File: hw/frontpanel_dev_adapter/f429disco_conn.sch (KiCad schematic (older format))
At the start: 7 parts, among them J601 Conn_02x32_Odd_Even, J602 Conn_02x32_Odd_Even, J603 Conn_02x32_Odd_Even, J604 Conn_02x32_Odd_Even

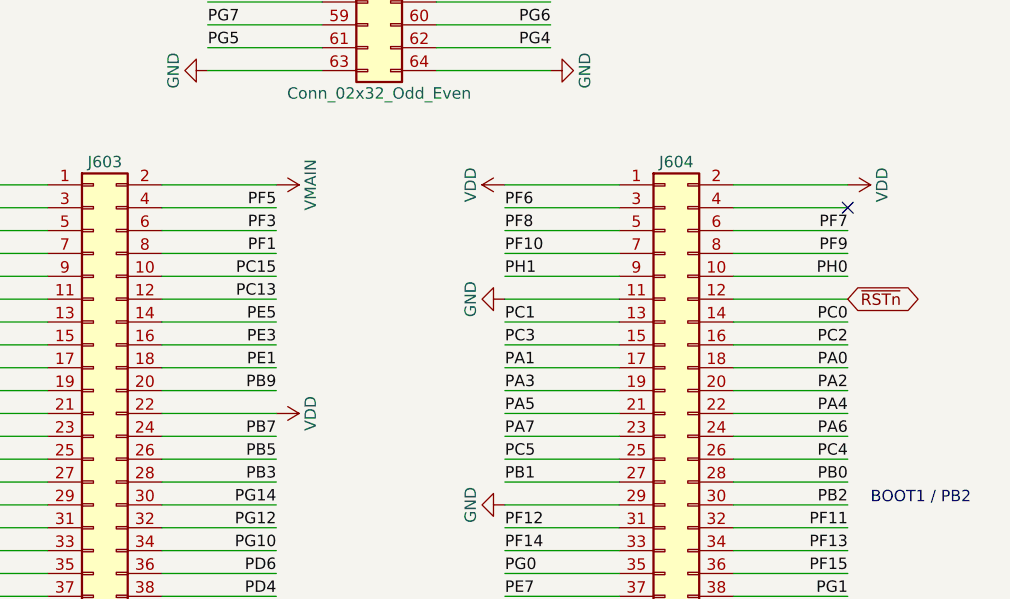
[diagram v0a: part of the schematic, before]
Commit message: "Frontpanel dev-adapter: change some component sizes, add Logo & 4x mounting holes"
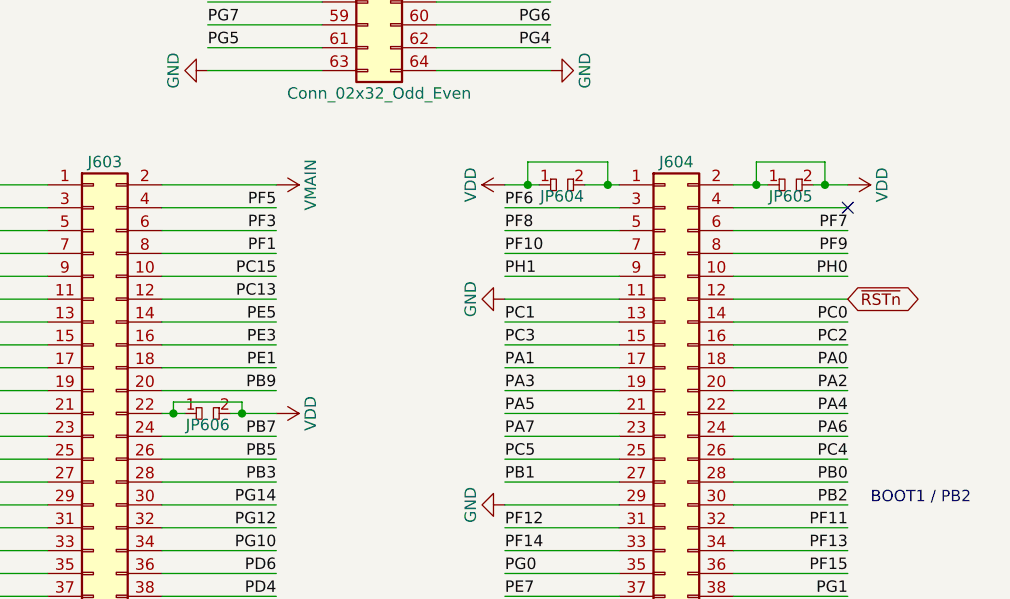
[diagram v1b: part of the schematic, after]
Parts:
- added JP604, JP605, JP606: dogbone_2_ud, customlib_mj_fp:db2_ud_0402, symbol customlib_mj:dogbone_2_ud
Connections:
- net VDD: now also JP604.1, JP604.2, JP605.1, JP605.2, JP606.1, JP606.2
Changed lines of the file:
@@
 	2350 5300 2850 5300
 Wire Wire Line
-	2350 5400 2850 5400
-Wire Wire Line
 	2350 5500 2850 5500
 Wire Wire Line
@@
 	2350 7500 2850 7500
 Wire Wire Line
-	4350 4400 3850 4400
-Wire Wire Line
 	4350 4500 3850 4500
 Wire Wire Line
@@
 Wire Wire Line
 	4350 7500 3850 7500
-Wire Wire Line
-	4850 4400 5350 4400
 Wire Wire Line
 	4850 4600 5350 4600
@@
 Wire Wire Line
 	8850 800  9000 800
+$Comp
+L customlib_mj:dogbone_2_ud JP604
+U 1 1 5FE9A9E3
+P 4100 4400
+F 0 "JP604" H 4100 4350 50  0000 C CNN
+F 1 "dogbone_2_ud" H 4100 4500 50  0001 C CNN
+F 2 "customlib_mj_fp:db2_ud_0402" H 4100 4400 50  0001 C CNN
+F 3 "" H 4100 4400 50  0001 C CNN
+	1    4100 4400
+	1    0    0    -1
+$EndComp
+$Comp
+L customlib_mj:dogbone_2_ud JP605
+U 1 1 5FE9B7C0
+P 5100 4400
+F 0 "JP605" H 5100 4350 50  0000 C CNN
+F 1 "dogbone_2_ud" H 5100 4500 50  0001 C CNN
+F 2 "customlib_mj_fp:db2_ud_0402" H 5100 4400 50  0001 C CNN
+F 3 "" H 5100 4400 50  0001 C CNN
+	1    5100 4400
+	1    0    0    -1
+$EndComp
+Wire Wire Line
+	4850 4400 4950 4400
+Wire Wire Line
+	4350 4400 4300 4400
+Wire Wire Line
+	3850 4400 3950 4400
+Wire Wire Line
+	3950 4400 3950 4300
+Wire Wire Line
+	3950 4300 4300 4300
+Wire Wire Line
+	4300 4300 4300 4400
+Connection ~ 3950 4400
+Wire Wire Line
+	3950 4400 4000 4400
+Connection ~ 4300 4400
+Wire Wire Line
+	4300 4400 4200 4400
+Wire Wire Line
+	5350 4400 5250 4400
+Wire Wire Line
+	5250 4400 5250 4300
+Wire Wire Line
+	5250 4300 4950 4300
+Wire Wire Line
+	4950 4300 4950 4400
+Connection ~ 5250 4400
+Wire Wire Line
+	5250 4400 5200 4400
+Connection ~ 4950 4400
+Wire Wire Line
+	4950 4400 5000 4400
+$Comp
+L customlib_mj:dogbone_2_ud JP606
+U 1 1 5FFA3733
+P 2550 5400
+F 0 "JP606" H 2550 5350 50  0000 C CNN
+F 1 "dogbone_2_ud" H 2550 5500 50  0001 C CNN
+F 2 "customlib_mj_fp:db2_ud_0402" H 2550 5400 50  0001 C CNN
+F 3 "" H 2550 5400 50  0001 C CNN
+	1    2550 5400
+	1    0    0    -1
+$EndComp
+Wire Wire Line
+	2450 5400 2400 5400
+Wire Wire Line
+	2650 5400 2700 5400
+Wire Wire Line
+	2400 5400 2400 5350
+Wire Wire Line
+	2400 5350 2700 5350
+Wire Wire Line
+	2700 5350 2700 5400
+Connection ~ 2400 5400
+Wire Wire Line
+	2400 5400 2350 5400
+Connection ~ 2700 5400
+Wire Wire Line
+	2700 5400 2850 5400
 $EndSCHEMATC

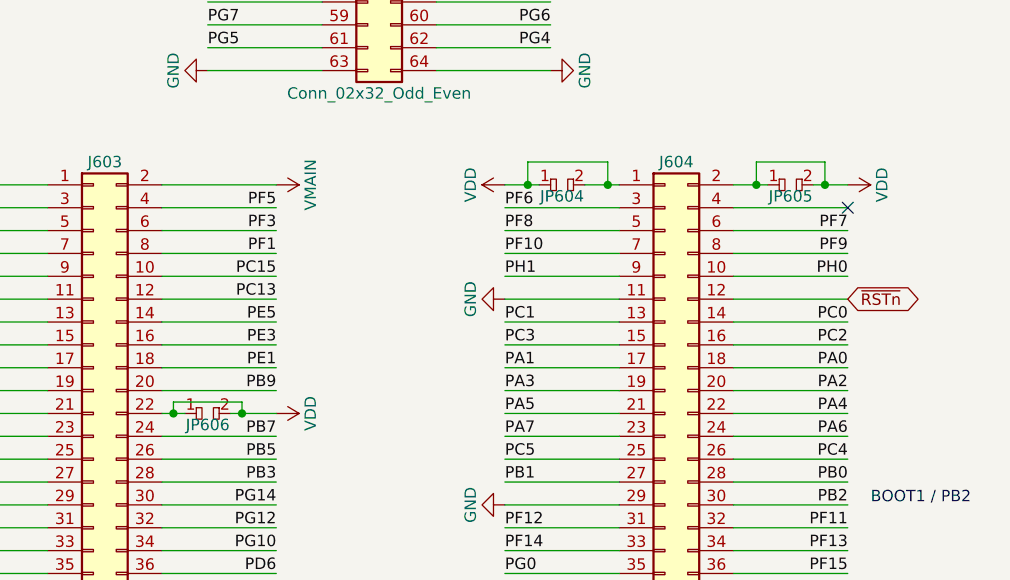
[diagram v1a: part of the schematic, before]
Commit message: FP adapter/devboard: some initial routing
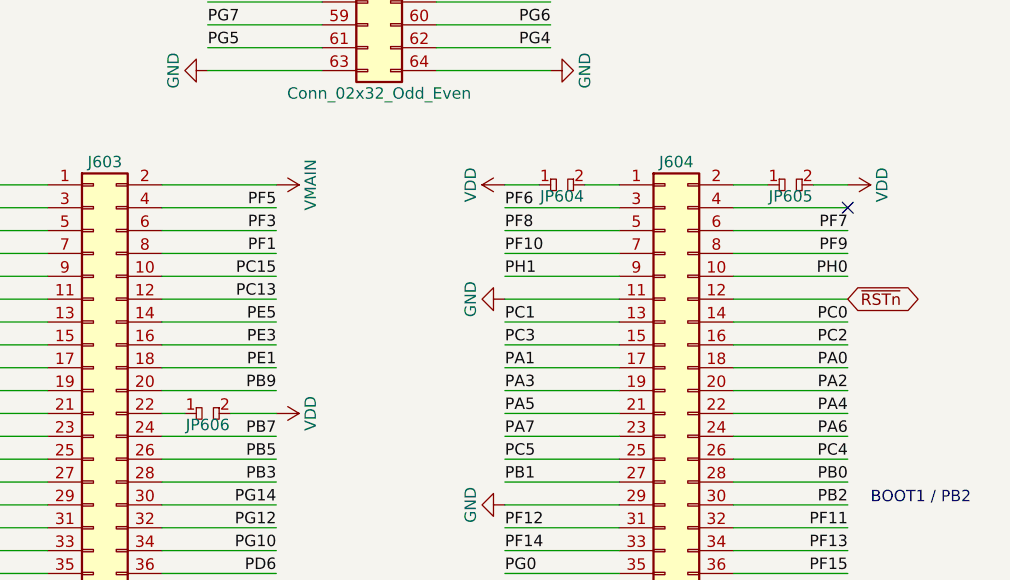
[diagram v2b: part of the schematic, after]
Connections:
- net VDD: no longer J603.22 (Pin_22), J604.1 (Pin_1), J604.2 (Pin_2), JP604.2, JP605.1, JP606.1
- new net: J604.1 (Pin_1), JP604.2
- new net: J604.2 (Pin_2), JP605.1
- new net: J603.22 (Pin_22), JP606.1
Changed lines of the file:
@@
 	1    0    0    -1
 $EndComp
-Wire Wire Line
-	4850 4400 4950 4400
-Wire Wire Line
-	4350 4400 4300 4400
-Wire Wire Line
-	3850 4400 3950 4400
-Wire Wire Line
-	3950 4400 3950 4300
-Wire Wire Line
-	3950 4300 4300 4300
-Wire Wire Line
-	4300 4300 4300 4400
-Connection ~ 3950 4400
-Wire Wire Line
-	3950 4400 4000 4400
-Connection ~ 4300 4400
-Wire Wire Line
-	4300 4400 4200 4400
-Wire Wire Line
-	5350 4400 5250 4400
-Wire Wire Line
-	5250 4400 5250 4300
-Wire Wire Line
-	5250 4300 4950 4300
-Wire Wire Line
-	4950 4300 4950 4400
-Connection ~ 5250 4400
-Wire Wire Line
-	5250 4400 5200 4400
-Connection ~ 4950 4400
-Wire Wire Line
-	4950 4400 5000 4400
 $Comp
 L customlib_mj:dogbone_2_ud JP606
@@
 $EndComp
 Wire Wire Line
-	2450 5400 2400 5400
+	4850 4400 5000 4400
 Wire Wire Line
-	2650 5400 2700 5400
+	5200 4400 5350 4400
 Wire Wire Line
-	2400 5400 2400 5350
+	4200 4400 4350 4400
 Wire Wire Line
-	2400 5350 2700 5350
+	3850 4400 4000 4400
 Wire Wire Line
-	2700 5350 2700 5400
-Connection ~ 2400 5400
+	2350 5400 2450 5400
 Wire Wire Line
-	2400 5400 2350 5400
-Connection ~ 2700 5400
-Wire Wire Line
-	2700 5400 2850 5400
+	2650 5400 2850 5400
 $EndSCHEMATC

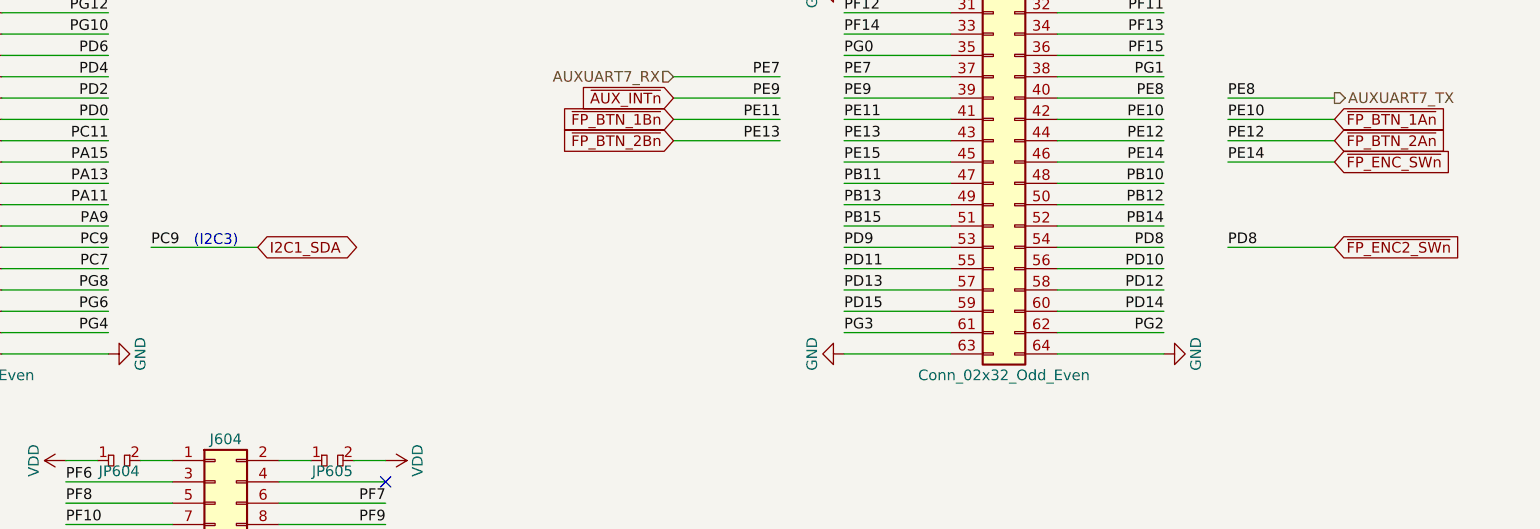
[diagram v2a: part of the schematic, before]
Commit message: FP adapter/dev board: *routing DONE* ; minor pinout tweaks (optimize routing); fix some missing 3d models
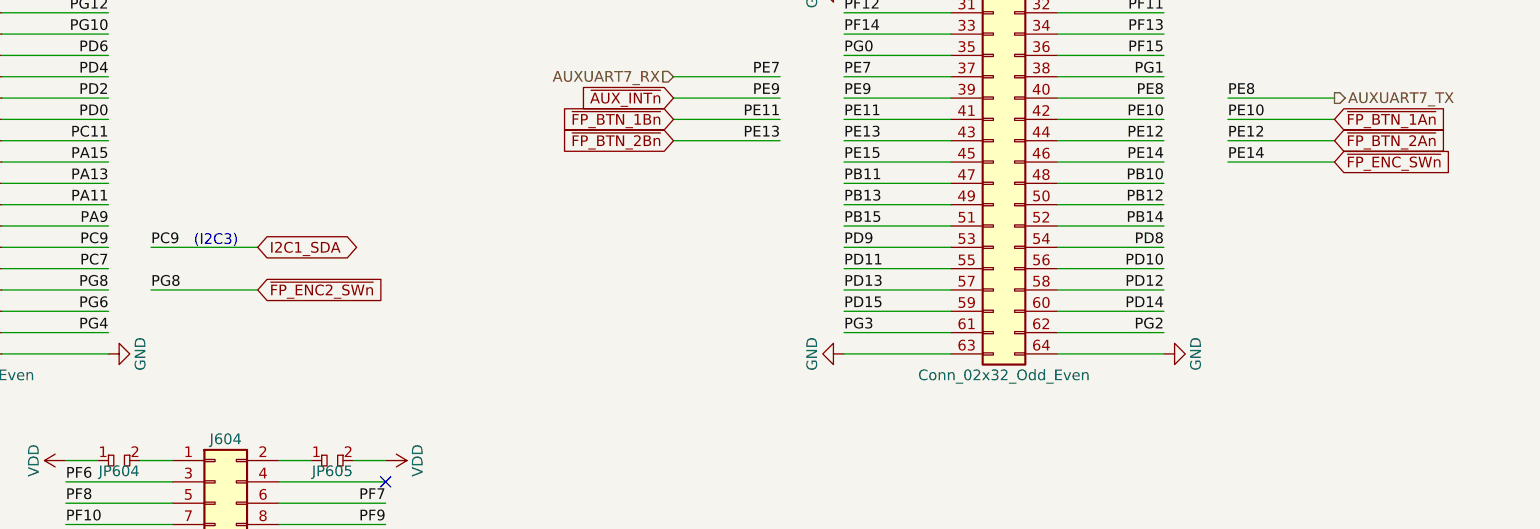
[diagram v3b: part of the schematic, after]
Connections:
- net PG8 is gone; now on net ~FP_ENC2_SWn~: J601.58 (Pin_58), J603.58 (Pin_58)
- net ~FP_ENC2_SWn~: no longer J602.54 (Pin_54), J604.54 (Pin_54)
- new net PD8: J602.54 (Pin_54), J604.54 (Pin_54)
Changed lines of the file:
@@
 Text Label 2350 1000 2    50   ~ 0
 PF2
-Text GLabel 9800 3400 2    50   Input ~ 0
+Text GLabel 4750 3600 2    50   Input ~ 0
 ~FP_ENC2_SWn~
 Text Label 9300 1400 0    50   ~ 0
@@
 PE13
 Wire Wire Line
-	9300 3400 9800 3400
-Text Label 9300 3400 0    50   ~ 0
-PD8
+	4250 3600 4750 3600
 Text Label 2400 2000 2    50   ~ 0
 PB4
@@
 Wire Wire Line
 	2650 5400 2850 5400
+Text Label 4250 3600 0    50   ~ 0
+PG8
 $EndSCHEMATC
